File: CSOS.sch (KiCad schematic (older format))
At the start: 10 parts

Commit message: Updating the schematic with part numbers.
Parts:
- removed U?: TC1016, symbol TC1016
- added C?: C, symbol C
- added R?: 0, symbol R
- added U?: TC1016, symbol TC1016
- Q1: renamed from Q?; value Q_NMOS_DGS -> BUK9575; MPN (none) -> BUK9575-100A,127
- R2: renamed from R?; value R -> .1; MPN (none) -> AC01000001007JA100
- gave numbers to parts that had none: 6
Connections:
- net labels added: 2.7V
- wire segments 28 -> 33
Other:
- moved on the sheet: C1, C2, P1, Q1, R2
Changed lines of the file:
@@
 LIBS:valves
 LIBS:CSOS
+LIBS:CSOS-cache
 EELAYER 25 0
 EELAYER END
@@
 $EndDescr
 $Comp
-L LMV358 U?
+L LMV358 U1
 U 1 1 57477267
 P 5710 4160
-F 0 "U?" H 5660 4360 50  0000 L CNN
+F 0 "U1" H 5660 4360 50  0000 L CNN
 F 1 "LMV358" H 5660 3910 50  0000 L CNN
 F 2 "" H 5710 4160 50  0000 C CNN
@@
 $EndComp
 $Comp
-L R R?
+L R R2
 U 1 1 574773EF
-P 6680 4770
-F 0 "R?" V 6760 4770 50  0000 C CNN
-F 1 "R" V 6680 4770 50  0000 C CNN
-F 2 "" V 6610 4770 50  0000 C CNN
-F 3 "" H 6680 4770 50  0000 C CNN
-	1    6680 4770
-	1    0    0    -1
-$EndComp
-$Comp
-L GND #PWR?
+P 7230 5140
+F 0 "R2" V 7310 5140 50  0000 C CNN
+F 1 ".1" V 7230 5140 50  0000 C CNN
+F 2 "" V 7160 5140 50  0000 C CNN
+F 3 "" H 7230 5140 50  0000 C CNN
+F 4 "AC01000001007JA100" V 7230 5140 60  0001 C CNN "MPN"
+	1    7230 5140
+	1    0    0    -1
+$EndComp
+$Comp
+L GND #PWR3
 U 1 1 574775C6
-P 6680 5210
-F 0 "#PWR?" H 6680 4960 50  0001 C CNN
-F 1 "GND" H 6680 5060 50  0000 C CNN
-F 2 "" H 6680 5210 50  0000 C CNN
-F 3 "" H 6680 5210 50  0000 C CNN
-	1    6680 5210
-	1    0    0    -1
-$EndComp
-$Comp
-L Q_NMOS_DGS Q?
+P 7230 5580
+F 0 "#PWR3" H 7230 5330 50  0001 C CNN
+F 1 "GND" H 7230 5430 50  0000 C CNN
+F 2 "" H 7230 5580 50  0000 C CNN
+F 3 "" H 7230 5580 50  0000 C CNN
+	1    7230 5580
+	1    0    0    -1
+$EndComp
+$Comp
+L Q_NMOS_DGS Q1
 U 1 1 574775E0
-P 6580 4160
-F 0 "Q?" H 6880 4210 50  0000 R CNN
-F 1 "Q_NMOS_DGS" H 7230 4110 50  0000 R CNN
-F 2 "" H 6780 4260 50  0000 C CNN
-F 3 "" H 6580 4160 50  0000 C CNN
-	1    6580 4160
-	1    0    0    -1
-$EndComp
-$Comp
-L R R?
+P 7130 4160
+F 0 "Q1" H 7430 4210 50  0000 R CNN
+F 1 "BUK9575" H 7780 4110 50  0000 R CNN
+F 2 "" H 7330 4260 50  0000 C CNN
+F 3 "" H 7130 4160 50  0000 C CNN
+F 4 "BUK9575-100A,127 " H 7130 4160 60  0001 C CNN "MPN"
+	1    7130 4160
+	1    0    0    -1
+$EndComp
+$Comp
+L R R1
 U 1 1 57477CA4
 P 4600 4650
-F 0 "R?" V 4680 4650 50  0000 C CNN
+F 0 "R1" V 4680 4650 50  0000 C CNN
 F 1 "R" V 4600 4650 50  0000 C CNN
 F 2 "" V 4530 4650 50  0000 C CNN
@@
 $EndComp
 $Comp
-L GND #PWR?
+L GND #PWR1
 U 1 1 5747834C
 P 5610 4570
-F 0 "#PWR?" H 5610 4320 50  0001 C CNN
+F 0 "#PWR1" H 5610 4320 50  0001 C CNN
 F 1 "GND" H 5610 4420 50  0000 C CNN
 F 2 "" H 5610 4570 50  0000 C CNN
@@
 $EndComp
 $Comp
-L TC1016 U?
-U 1 1 574790E0
-P 6160 3130
-F 0 "U?" H 6310 2934 50  0000 C CNN
-F 1 "TC1016" H 6160 3330 50  0000 C CNN
-F 2 "" H 6160 3130 50  0000 C CNN
-F 3 "" H 6160 3130 50  0000 C CNN
-	1    6160 3130
-	-1   0    0    -1
-$EndComp
-$Comp
-L GND #PWR?
+L GND #PWR2
 U 1 1 57479315
 P 6160 3550
-F 0 "#PWR?" H 6160 3300 50  0001 C CNN
+F 0 "#PWR2" H 6160 3300 50  0001 C CNN
 F 1 "GND" H 6160 3400 50  0000 C CNN
 F 2 "" H 6160 3550 50  0000 C CNN
@@
 $EndComp
 $Comp
-L C C?
+L C C1
 U 1 1 574795A3
-P 5730 3330
-F 0 "C?" H 5755 3430 50  0000 L CNN
-F 1 "C" H 5755 3230 50  0000 L CNN
-F 2 "" H 5768 3180 50  0000 C CNN
-F 3 "" H 5730 3330 50  0000 C CNN
-	1    5730 3330
-	1    0    0    -1
-$EndComp
-$Comp
-L C C?
+P 5490 3060
+F 0 "C1" H 5515 3160 50  0000 L CNN
+F 1 "C" H 5515 2960 50  0000 L CNN
+F 2 "" H 5528 2910 50  0000 C CNN
+F 3 "" H 5490 3060 50  0000 C CNN
+	1    5490 3060
+	1    0    0    -1
+$EndComp
+$Comp
+L C C2
 U 1 1 5747972B
-P 6570 3320
-F 0 "C?" H 6595 3420 50  0000 L CNN
-F 1 "C" H 6595 3220 50  0000 L CNN
-F 2 "" H 6608 3170 50  0000 C CNN
-F 3 "" H 6570 3320 50  0000 C CNN
-	1    6570 3320
-	1    0    0    -1
-$EndComp
-Wire Wire Line
-	6680 4360 6680 5200
-Wire Wire Line
-	6680 4500 6380 4500
-Wire Wire Line
-	6380 4500 6380 4790
-Wire Wire Line
-	6380 4790 5180 4790
-Wire Wire Line
-	5180 4790 5180 4260
-Wire Wire Line
-	5180 4260 5410 4260
-Connection ~ 6680 4500
-Wire Wire Line
-	5610 4460 5610 4570
-Wire Wire Line
-	6010 4160 6380 4160
-Wire Wire Line
-	5410 4060 4930 4060
-Wire Wire Line
-	4930 4060 4930 4380
-Wire Wire Line
-	4600 4280 4600 4500
-Wire Wire Line
-	4930 4380 4600 4380
-Connection ~ 4600 4380
-Wire Wire Line
-	6560 3080 7490 3080
-Wire Wire Line
-	5610 3080 5610 3860
-Wire Wire Line
-	4600 4800 4600 5040
-Wire Wire Line
-	4600 5040 6680 5040
-Connection ~ 6680 5040
-Connection ~ 5610 3080
-Wire Wire Line
-	6160 3380 6160 3550
-Wire Wire Line
-	6680 3080 6680 3960
-Connection ~ 6680 3080
-Wire Wire Line
-	6570 3170 6570 3080
-Wire Wire Line
-	6570 3080 6580 3080
-Connection ~ 6580 3080
-Wire Wire Line
-	5730 3180 5730 3080
-Connection ~ 5730 3080
-Wire Wire Line
-	5730 3480 6160 3480
-Connection ~ 6160 3480
-Wire Wire Line
-	6570 3470 6570 3520
-Wire Wire Line
-	6570 3520 6160 3520
-Connection ~ 6160 3520
-$Comp
-L POT RV?
+P 7010 2960
+F 0 "C2" H 7035 3060 50  0000 L CNN
+F 1 "C" H 7035 2860 50  0000 L CNN
+F 2 "" H 7048 2810 50  0000 C CNN
+F 3 "" H 7010 2960 50  0000 C CNN
+	1    7010 2960
+	1    0    0    -1
+$EndComp
+$Comp
+L POT RV1
 U 1 1 57479CE3
 P 4600 4030
-F 0 "RV?" H 4600 3930 50  0000 C CNN
+F 0 "RV1" H 4600 3930 50  0000 C CNN
 F 1 "POT" H 4600 4030 50  0000 C CNN
 F 2 "" H 4600 4030 50  0000 C CNN
@@
 	0    1    1    0
 $EndComp
-Wire Wire Line
-	4750 4030 4750 3080
-Connection ~ 4750 3080
-$Comp
-L CONN_01X02 P?
+$Comp
+L CONN_01X02 P1
 U 1 1 5747A1AB
-P 7690 3130
-F 0 "P?" H 7690 3280 50  0000 C CNN
-F 1 "CONN_01X02" V 7790 3130 50  0000 C CNN
-F 2 "" H 7690 3130 50  0000 C CNN
-F 3 "" H 7690 3130 50  0000 C CNN
-	1    7690 3130
-	1    0    0    -1
-$EndComp
-$Comp
-L GND #PWR?
+P 7600 2710
+F 0 "P1" H 7600 2860 50  0000 C CNN
+F 1 "CONN_01X02" V 7700 2710 50  0000 C CNN
+F 2 "" H 7600 2710 50  0000 C CNN
+F 3 "" H 7600 2710 50  0000 C CNN
+	1    7600 2710
+	1    0    0    -1
+$EndComp
+$Comp
+L GND #PWR4
 U 1 1 5747A301
 P 7400 3350
-F 0 "#PWR?" H 7400 3100 50  0001 C CNN
+F 0 "#PWR4" H 7400 3100 50  0001 C CNN
 F 1 "GND" H 7400 3200 50  0000 C CNN
 F 2 "" H 7400 3350 50  0000 C CNN
@@
 	1    0    0    -1
 $EndComp
-Wire Wire Line
-	7490 3180 7400 3180
-Wire Wire Line
-	7400 3180 7400 3350
-Wire Wire Line
-	4750 3080 5760 3080
-$Comp
-L LMV358 U?
+$Comp
+L LMV358 U1
 U 2 1 5747B322
 P 8210 5030
-F 0 "U?" H 8160 5230 50  0000 L CNN
+F 0 "U1" H 8160 5230 50  0000 L CNN
 F 1 "LMV358" H 8160 4780 50  0000 L CNN
 F 2 "" H 8210 5030 50  0000 C CNN
@@
 	1    0    0    -1
 $EndComp
+$Comp
+L TC1016 U?
+U 1 1 5749CEE7
+P 6160 2870
+F 0 "U?" H 6310 2674 50  0000 C CNN
+F 1 "TC1016" H 6160 3230 50  0000 C CNN
+F 2 "" H 6160 2870 50  0000 C CNN
+F 3 "" H 6160 2870 50  0000 C CNN
+	1    6160 2870
+	-1   0    0    -1
+$EndComp
+$Comp
+L R R?
+U 1 1 5749E988
+P 6780 2930
+F 0 "R?" V 6860 2930 50  0000 C CNN
+F 1 "0" V 6780 2930 50  0000 C CNN
+F 2 "" V 6710 2930 50  0000 C CNN
+F 3 "" H 6780 2930 50  0000 C CNN
+	1    6780 2930
+	1    0    0    -1
+$EndComp
+Connection ~ 6160 3300
+Wire Wire Line
+	5490 3300 6160 3300
+Wire Wire Line
+	5490 3210 5490 3300
+Wire Wire Line
+	5610 3380 5610 3860
+Wire Wire Line
+	4750 3380 5610 3380
+Wire Wire Line
+	6160 3520 7010 3520
+Wire Wire Line
+	7010 3520 7010 3110
+Wire Wire Line
+	6560 3180 6560 2830
+Wire Wire Line
+	6780 3180 6560 3180
+Wire Wire Line
+	6780 3080 6780 3180
+Connection ~ 6780 2660
+Wire Wire Line
+	6780 2780 6780 2660
+Connection ~ 7010 2660
+Wire Wire Line
+	7010 2660 7010 2810
+Wire Wire Line
+	7230 5290 7230 5580
+Wire Wire Line
+	7230 4360 7230 4990
+Wire Wire Line
+	4750 2660 5760 2660
+Wire Wire Line
+	7400 2760 7400 3350
+Connection ~ 4750 2660
+Wire Wire Line
+	4750 2660 4750 4030
+Connection ~ 6160 3520
+Connection ~ 5490 2660
+Wire Wire Line
+	5490 2660 5490 2910
+Connection ~ 7230 2660
+Wire Wire Line
+	7230 2660 7230 3960
+Wire Wire Line
+	6160 3130 6160 3550
+Connection ~ 7230 5410
+Wire Wire Line
+	4600 5410 7230 5410
+Wire Wire Line
+	6560 2660 7400 2660
+Connection ~ 4600 4380
+Wire Wire Line
+	4930 4380 4600 4380
+Wire Wire Line
+	4600 4280 4600 4500
+Wire Wire Line
+	4930 4060 4930 4380
+Wire Wire Line
+	5410 4060 4930 4060
+Wire Wire Line
+	5610 4460 5610 4570
+Wire Wire Line
+	5180 4260 5410 4260
+Wire Wire Line
+	5180 4790 5180 4260
+Wire Wire Line
+	5180 4790 7230 4790
+Connection ~ 4750 3380
+Wire Wire Line
+	6010 4160 6930 4160
+$Comp
+L C C?
+U 1 1 574A0852
+P 5260 3610
+F 0 "C?" H 5285 3710 50  0000 L CNN
+F 1 "C" H 5285 3510 50  0000 L CNN
+F 2 "" H 5298 3460 50  0000 C CNN
+F 3 "" H 5260 3610 50  0000 C CNN
+	1    5260 3610
+	1    0    0    -1
+$EndComp
+$Comp
+L GND #PWR?
+U 1 1 574A08FE
+P 5260 3800
+F 0 "#PWR?" H 5260 3550 50  0001 C CNN
+F 1 "GND" H 5260 3650 50  0000 C CNN
+F 2 "" H 5260 3800 50  0000 C CNN
+F 3 "" H 5260 3800 50  0000 C CNN
+	1    5260 3800
+	1    0    0    -1
+$EndComp
+Wire Wire Line
+	5260 3460 5260 3380
+Connection ~ 5260 3380
+Wire Wire Line
+	5260 3800 5260 3760
+Wire Wire Line
+	4600 4800 4600 5410
+Text Label 4910 3380 0    60   ~ 0
+2.7V
+Connection ~ 7230 4790
 $EndSCHEMATC

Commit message: Upgrading linear regulator.
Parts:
- removed U?: TC1016, symbol TC1016
- added P?: CONN_01X03, symbol CONN_01X03
- added P?: CONN_01X02, symbol CONN_01X02
- added R?: 27K, symbol R
- added R?: 21.6K, symbol R
- added U?: LM2931D-R, symbol LM2931D-R
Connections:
- wire segments 33 -> 53
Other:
- note added: "Battery Pack"
- note added: "Current Sink Input"
- moved on the sheet: C1
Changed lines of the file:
@@
 L C C1
 U 1 1 574795A3
-P 5490 3060
-F 0 "C1" H 5515 3160 50  0000 L CNN
-F 1 "C" H 5515 2960 50  0000 L CNN
-F 2 "" H 5528 2910 50  0000 C CNN
-F 3 "" H 5490 3060 50  0000 C CNN
-	1    5490 3060
+P 5290 3060
+F 0 "C1" H 5315 3160 50  0000 L CNN
+F 1 "C" H 5315 2960 50  0000 L CNN
+F 2 "" H 5328 2910 50  0000 C CNN
+F 3 "" H 5290 3060 50  0000 C CNN
+	1    5290 3060
 	1    0    0    -1
 $EndComp
@@
 $EndComp
 $Comp
-L TC1016 U?
-U 1 1 5749CEE7
-P 6160 2870
-F 0 "U?" H 6310 2674 50  0000 C CNN
-F 1 "TC1016" H 6160 3230 50  0000 C CNN
-F 2 "" H 6160 2870 50  0000 C CNN
-F 3 "" H 6160 2870 50  0000 C CNN
-	1    6160 2870
-	-1   0    0    -1
-$EndComp
-$Comp
 L R R?
 U 1 1 5749E988
@@
 Connection ~ 6160 3300
 Wire Wire Line
-	5490 3300 6160 3300
-Wire Wire Line
-	5490 3210 5490 3300
+	5290 3300 6160 3300
+Wire Wire Line
+	5290 3210 5290 3300
 Wire Wire Line
 	5610 3380 5610 3860
@@
 Wire Wire Line
 	7010 3520 7010 3110
-Wire Wire Line
-	6560 3180 6560 2830
-Wire Wire Line
-	6780 3180 6560 3180
-Wire Wire Line
-	6780 3080 6780 3180
-Connection ~ 6780 2660
-Wire Wire Line
-	6780 2780 6780 2660
-Connection ~ 7010 2660
-Wire Wire Line
-	7010 2660 7010 2810
+Connection ~ 7010 2320
+Wire Wire Line
+	7010 2320 7010 2810
 Wire Wire Line
 	7230 5290 7230 5580
@@
 	7230 4360 7230 4990
 Wire Wire Line
-	4750 2660 5760 2660
+	4750 2320 5810 2320
 Wire Wire Line
 	7400 2760 7400 3350
-Connection ~ 4750 2660
-Wire Wire Line
-	4750 2660 4750 4030
+Connection ~ 4750 2320
+Wire Wire Line
+	4750 2320 4750 4030
 Connection ~ 6160 3520
-Connection ~ 5490 2660
-Wire Wire Line
-	5490 2660 5490 2910
-Connection ~ 7230 2660
-Wire Wire Line
-	7230 2660 7230 3960
-Wire Wire Line
-	6160 3130 6160 3550
+Wire Wire Line
+	7230 2170 7230 3960
+Wire Wire Line
+	6160 2880 6160 3550
 Connection ~ 7230 5410
 Wire Wire Line
 	4600 5410 7230 5410
-Wire Wire Line
-	6560 2660 7400 2660
 Connection ~ 4600 4380
 Wire Wire Line
@@
 2.7V
 Connection ~ 7230 4790
+$Comp
+L LM2931D-R U?
+U 1 1 574B9978
+P 6220 2520
+F 0 "U?" H 6490 2310 50  0000 C CNN
+F 1 "LM2931D-R" H 6240 2870 50  0000 C CNN
+F 2 "" H 6220 2520 50  0000 C CNN
+F 3 "" H 6220 2520 50  0000 C CNN
+	1    6220 2520
+	-1   0    0    -1
+$EndComp
+$Comp
+L R R?
+U 1 1 574BAC95
+P 5610 2580
+F 0 "R?" V 5690 2580 50  0000 C CNN
+F 1 "27K" V 5610 2580 50  0000 C CNN
+F 2 "" V 5540 2580 50  0000 C CNN
+F 3 "" H 5610 2580 50  0000 C CNN
+	1    5610 2580
+	1    0    0    -1
+$EndComp
+$Comp
+L R R?
+U 1 1 574BAD6B
+P 5610 2960
+F 0 "R?" V 5690 2960 50  0000 C CNN
+F 1 "21.6K" V 5610 2960 50  0000 C CNN
+F 2 "" V 5540 2960 50  0000 C CNN
+F 3 "" H 5610 2960 50  0000 C CNN
+	1    5610 2960
+	1    0    0    -1
+$EndComp
+Wire Wire Line
+	5290 2910 5290 2320
+Connection ~ 5290 2320
+Wire Wire Line
+	5610 2430 5610 2320
+Connection ~ 5610 2320
+Wire Wire Line
+	5610 2810 5610 2730
+Wire Wire Line
+	5610 3110 5610 3300
+Connection ~ 5610 3300
+Wire Wire Line
+	5610 2770 5750 2770
+Wire Wire Line
+	5750 2770 5750 2440
+Wire Wire Line
+	5750 2440 5810 2440
+Connection ~ 5610 2770
+Wire Wire Line
+	7310 2320 7310 2660
+Wire Wire Line
+	7310 2660 7400 2660
+Wire Wire Line
+	6600 2440 6780 2440
+Wire Wire Line
+	6780 2440 6780 2780
+Wire Wire Line
+	6780 3080 6780 3520
+Connection ~ 6780 3520
+Wire Wire Line
+	6320 2880 6320 3520
+Connection ~ 6320 3520
+Wire Wire Line
+	6240 2880 6240 3520
+Connection ~ 6240 3520
+Wire Wire Line
+	6080 2880 6080 3300
+Connection ~ 6080 3300
+$Comp
+L CONN_01X03 P?
+U 1 1 574C18ED
+P 7130 1970
+F 0 "P?" H 7130 2170 50  0000 C CNN
+F 1 "CONN_01X03" V 7230 1970 50  0000 C CNN
+F 2 "" H 7130 1970 50  0000 C CNN
+F 3 "" H 7130 1970 50  0000 C CNN
+	1    7130 1970
+	0    -1   -1   0
+$EndComp
+Wire Wire Line
+	7310 2320 7230 2320
+Connection ~ 7230 2320
+Wire Wire Line
+	6600 2320 7130 2320
+Wire Wire Line
+	7130 2320 7130 2170
+Wire Wire Line
+	7030 2170 7030 2240
+Wire Wire Line
+	7030 2240 6680 2240
+$Comp
+L CONN_01X02 P?
+U 1 1 574C4DEE
+P 4010 2420
+F 0 "P?" H 4010 2570 50  0000 C CNN
+F 1 "CONN_01X02" V 4110 2420 50  0000 C CNN
+F 2 "" H 4010 2420 50  0000 C CNN
+F 3 "" H 4010 2420 50  0000 C CNN
+	1    4010 2420
+	0    1    1    0
+$EndComp
+Wire Wire Line
+	6680 2240 6680 2020
+Wire Wire Line
+	6680 2020 4060 2020
+Wire Wire Line
+	4060 2020 4060 2220
+$Comp
+L GND #PWR?
+U 1 1 574C54DB
+P 3360 2700
+F 0 "#PWR?" H 3360 2450 50  0001 C CNN
+F 1 "GND" H 3360 2550 50  0000 C CNN
+F 2 "" H 3360 2700 50  0000 C CNN
+F 3 "" H 3360 2700 50  0000 C CNN
+	1    3360 2700
+	1    0    0    -1
+$EndComp
+Wire Wire Line
+	3960 2210 3960 2020
+Wire Wire Line
+	3960 2020 3360 2020
+Wire Wire Line
+	3360 2020 3360 2700
+Text Notes 3730 2710 0    60   ~ 0
+Battery Pack
+Text Notes 7840 2720 0    60   ~ 0
+Current Sink Input
 $EndSCHEMATC

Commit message: Adding FET power SPICE sim.
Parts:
- RV1: symbol POT -> POT-RESCUE-CSOS
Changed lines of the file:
@@
 EESchema Schematic File Version 2
+LIBS:CSOS-rescue
 LIBS:power
 LIBS:device
@@
 $EndComp
 $Comp
-L POT RV1
+L POT-RESCUE-CSOS RV1
 U 1 1 57479CE3
 P 4600 4030

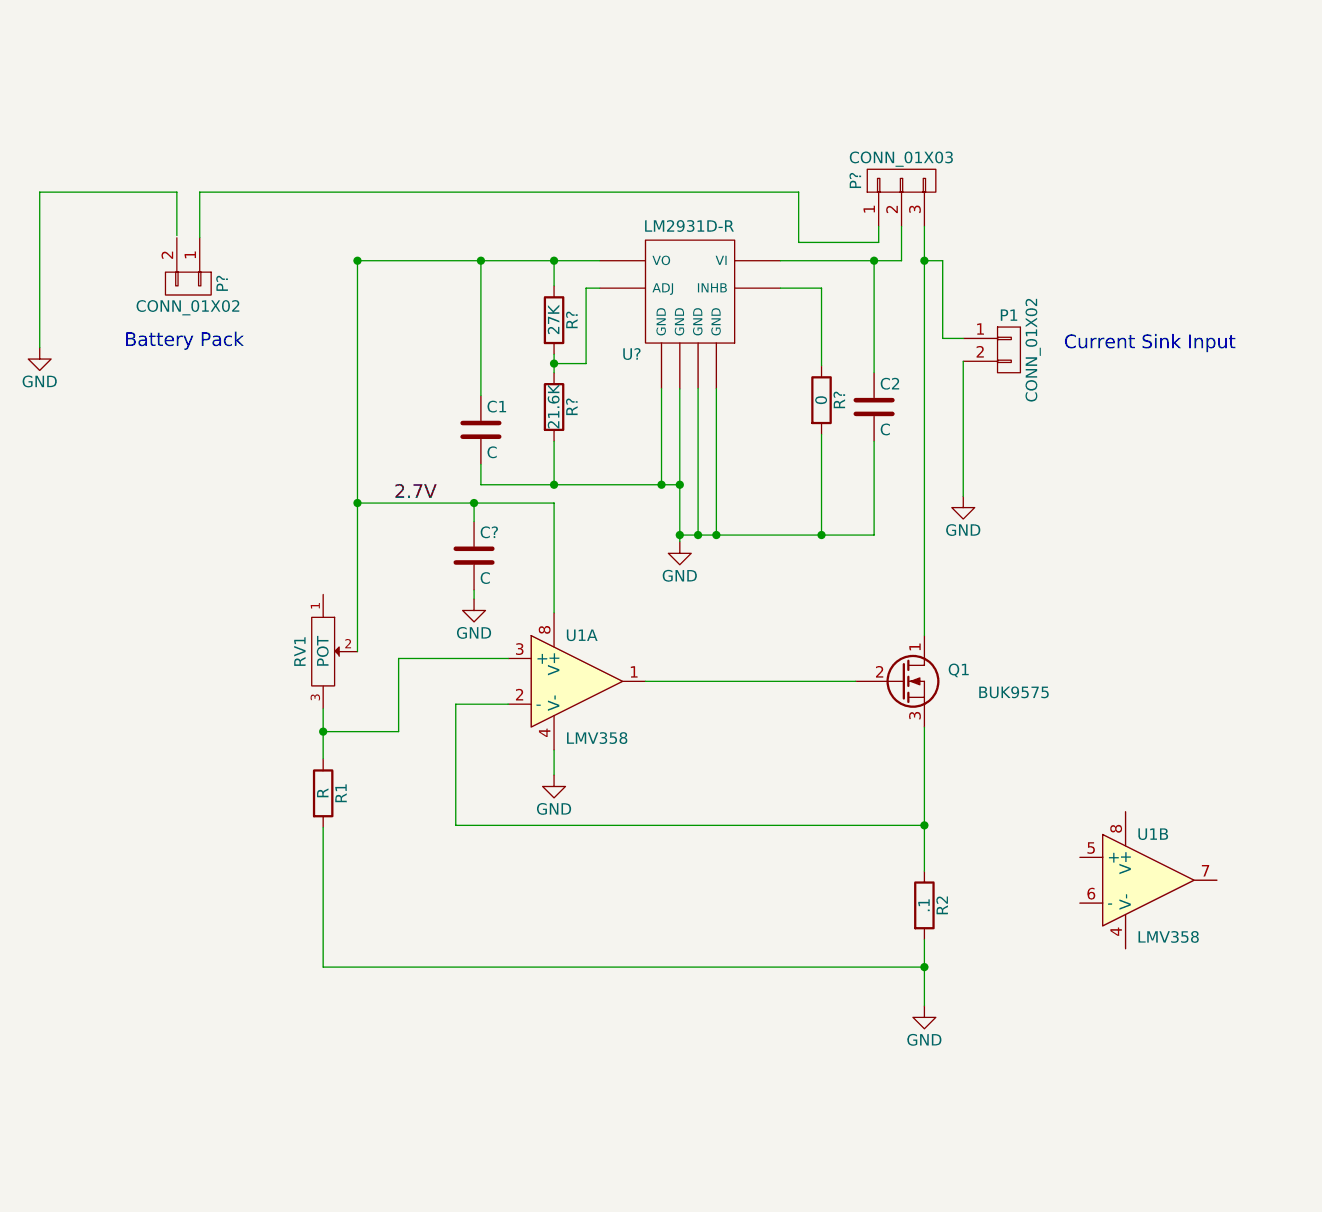
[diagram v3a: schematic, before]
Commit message: Adding hierarchical sheets and voltage regulation circuit.
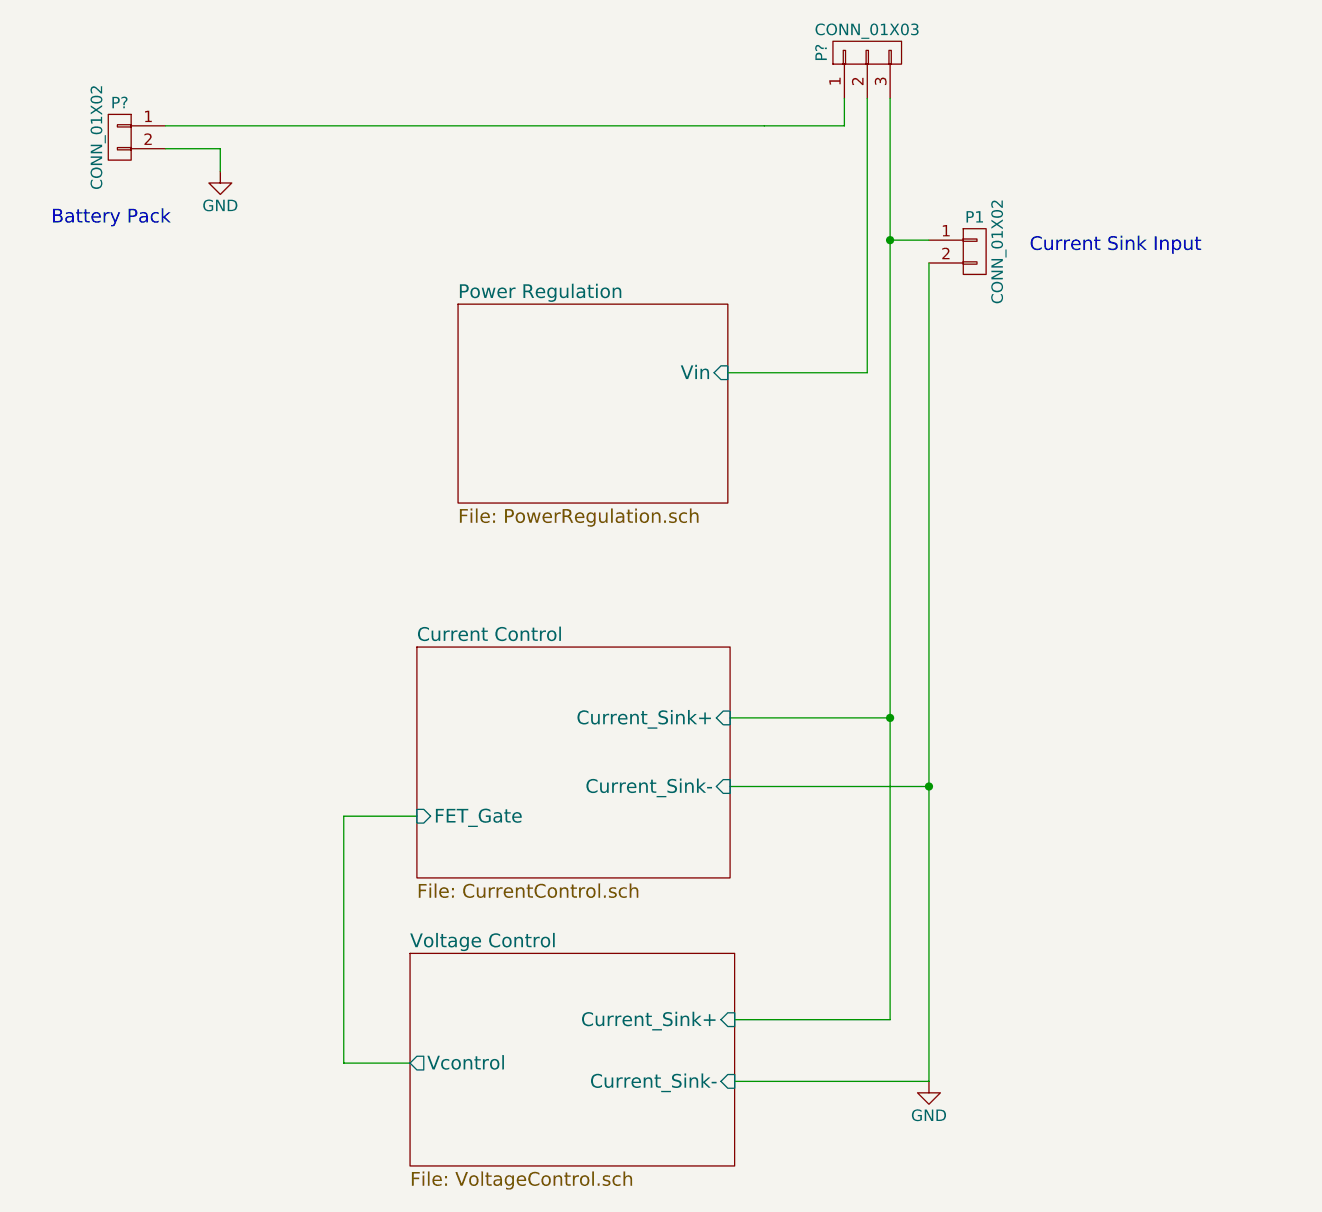
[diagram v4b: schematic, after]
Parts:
- removed C1, C2, C?: C, symbol C
- removed Q1: BUK9575, symbol Q_NMOS_DGS
- removed R1: R, symbol R
- removed R2: .1, symbol R
- removed R?: 0, symbol R
- removed R?: 27K, symbol R
- removed R?: 21.6K, symbol R
- removed RV1: POT, symbol POT-RESCUE-CSOS
- removed U1: LMV358, symbol LMV358
- removed U?: LM2931D-R, symbol LM2931D-R
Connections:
- net GND: now also P?.2 (P2)
- net Current Control/Current_Sink+: now reaches P1.1 (P1), P?.3 (P3)
- net Power Regulation/Vin: now reaches P?.2 (P2)
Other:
- moved on the sheet: P1, P?
